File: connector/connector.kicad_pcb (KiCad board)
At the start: 2 copper layers, 18.7 x 4.8 mm, 15 parts, among them P11 CONN_1, P12 CONN_1, P13 CONN_1, P14 CONN_1, P15 CONN_1, P21 CONN_1, P22 CONN_1, P23 CONN_1, P24 CONN_1, P25 CONN_1

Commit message: Set solder mask clearance to 0.
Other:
- rule pad_to_mask_clearance: 0.1016 -> 0
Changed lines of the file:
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@@
     (pad_size 0.6096 0.6096)
     (pad_drill 0.3556)
-    (pad_to_mask_clearance 0.1016)
+    (pad_to_mask_clearance 0)
     (aux_axis_origin 0 0)
     (visible_elements FFFFFF7F)
@@
   (gr_line (start 138.4 102.4) (end 140.4 102.4) (angle 90) (layer Edge.Cuts) (width 0.01))
   (gr_line (start 140.4 102.4) (end 140.4 100.8) (angle 90) (layer Edge.Cuts) (width 0.01))
+  (segment (start 141 99.3) (end 141.333333 99.633333) (width 0.733) (layer Front) (net 1))
+  (segment (start 141 98.95) (end 141 99.3) (width 0.733) (layer Front) (net 1))
+  (segment (start 141.983333 99.633333) (end 141.333333 99.633333) (width 0.733) (layer Back) (net 1))
   (segment (start 142.1 99.75) (end 141.983333 99.633333) (width 0.733) (layer Back) (net 1))
-  (segment (start 141.983333 99.633333) (end 141.333333 99.633333) (width 0.733) (layer Back) (net 1))
-  (segment (start 141 98.95) (end 141 99.3) (width 0.733) (layer Front) (net 1))
-  (segment (start 141 99.3) (end 141.333333 99.633333) (width 0.733) (layer Front) (net 1))
+  (segment (start 143.5 99.3) (end 143.833333 99.633333) (width 0.733) (layer Front) (net 2))
+  (segment (start 143.5 98.95) (end 143.5 99.3) (width 0.733) (layer Front) (net 2))
+  (segment (start 144.633333 99.633333) (end 143.833333 99.633333) (width 0.733) (layer Back) (net 2))
   (segment (start 144.75 99.75) (end 144.633333 99.633333) (width 0.733) (layer Back) (net 2))
-  (segment (start 144.633333 99.633333) (end 143.833333 99.633333) (width 0.733) (layer Back) (net 2))
-  (segment (start 143.5 98.95) (end 143.5 99.3) (width 0.733) (layer Front) (net 2))
-  (segment (start 143.5 99.3) (end 143.833333 99.633333) (width 0.733) (layer Front) (net 2))
+  (segment (start 146 99.3) (end 146.333333 99.633333) (width 0.733) (layer Front) (net 3))
+  (segment (start 146 98.95) (end 146 99.3) (width 0.733) (layer Front) (net 3))
+  (segment (start 147.283333 99.633333) (end 146.333333 99.633333) (width 0.733) (layer Back) (net 3))
   (segment (start 147.4 99.75) (end 147.283333 99.633333) (width 0.733) (layer Back) (net 3))
-  (segment (start 147.283333 99.633333) (end 146.333333 99.633333) (width 0.733) (layer Back) (net 3))
-  (segment (start 146 98.95) (end 146 99.3) (width 0.733) (layer Front) (net 3))
-  (segment (start 146 99.3) (end 146.333333 99.633333) (width 0.733) (layer Front) (net 3))
+  (segment (start 148.5 99.3) (end 148.833333 99.633333) (width 0.733) (layer Front) (net 4))
+  (segment (start 148.5 98.95) (end 148.5 99.3) (width 0.733) (layer Front) (net 4))
+  (segment (start 149.933333 99.633333) (end 148.833333 99.633333) (width 0.733) (layer Back) (net 4))
   (segment (start 150.05 99.75) (end 149.933333 99.633333) (width 0.733) (layer Back) (net 4))
-  (segment (start 149.933333 99.633333) (end 148.833333 99.633333) (width 0.733) (layer Back) (net 4))
-  (segment (start 148.5 98.95) (end 148.5 99.3) (width 0.733) (layer Front) (net 4))
-  (segment (start 148.5 99.3) (end 148.833333 99.633333) (width 0.733) (layer Front) (net 4))
+  (segment (start 151 99.299999) (end 151.333334 99.633333) (width 0.733) (layer Front) (net 5))
+  (segment (start 151 98.95) (end 151 99.299999) (width 0.733) (layer Front) (net 5))
+  (segment (start 152.583333 99.633333) (end 151.333334 99.633333) (width 0.733) (layer Back) (net 5))
   (segment (start 152.7 99.75) (end 152.583333 99.633333) (width 0.733) (layer Back) (net 5))
-  (segment (start 152.583333 99.633333) (end 151.333334 99.633333) (width 0.733) (layer Back) (net 5))
-  (segment (start 151 98.95) (end 151 99.299999) (width 0.733) (layer Front) (net 5))
-  (segment (start 151 99.299999) (end 151.333334 99.633333) (width 0.733) (layer Front) (net 5))
 )

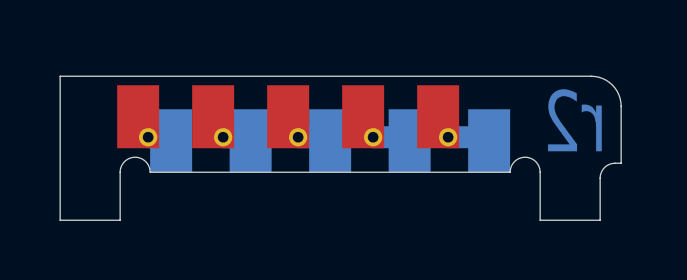
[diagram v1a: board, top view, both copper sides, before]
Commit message: Update outline.
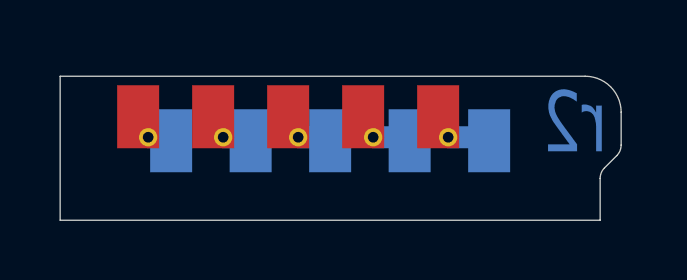
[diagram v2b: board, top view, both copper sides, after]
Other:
- outline, holes or cut-outs redrawn
- net class Default: clearance 0.01 -> 0.254; trace_width 0.889 -> 0.254
- rule trace_clearance: 0.01 -> 0.254
- rule trace_min: 0.6 -> 0.254
- rule via_min_drill: 0.635 -> 0.508

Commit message: Update pad positions.
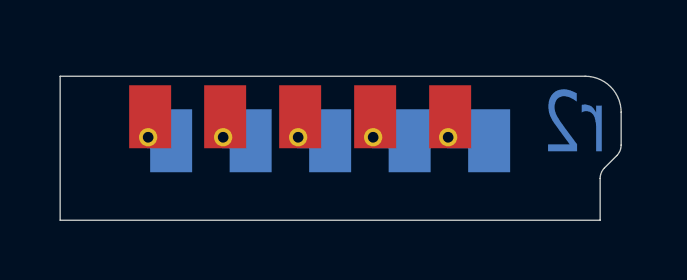
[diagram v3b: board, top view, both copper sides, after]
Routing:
- net N-000005: track 2.24 -> 1.41 mm
- net N-000003: track 1.94 -> 1.11 mm
- net N-000002: track 1.79 -> 0.96 mm
- net N-000001: track 1.64 -> 0.81 mm
- net N-000004: track 2.09 -> 1.26 mm
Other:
- rule pad_to_mask_clearance: 0 -> 0.254
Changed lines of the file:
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@@
     (thickness 1.6)
     (drawings 17)
-    (tracks 20)
+    (tracks 10)
     (zones 0)
     (modules 15)
@@
     (zone_45_only no)
     (trace_min 0.254)
-    (segment_width 0.2)
-    (edge_width 0.1)
+    (segment_width 0.381)
+    (edge_width 0.01016)
     (via_size 0.889)
     (via_drill 0.635)
@@
     (uvia_min_size 0.508)
     (uvia_min_drill 0.127)
-    (pcb_text_width 0.3)
-    (pcb_text_size 1.5 1.5)
-    (mod_edge_width 0.15)
-    (mod_text_size 1 1)
-    (mod_text_width 0.15)
-    (pad_size 1.5 1.5)
-    (pad_drill 0.6)
-    (pad_to_mask_clearance 0)
+    (pcb_text_width 0.3048)
+    (pcb_text_size 1.524 2.032)
+    (mod_edge_width 0.381)
+    (mod_text_size 1.524 1.524)
+    (mod_text_width 0.3048)
+    (pad_size 1.4 2.1)
+    (pad_drill 0)
+    (pad_to_mask_clearance 0.254)
     (aux_axis_origin 0 0)
     (visible_elements FFFFF77F)
@@
       (effects (font (thickness 0.3048)))
     )
-    (pad "" smd rect (at 0 0) (size 1.4 2.1) (layers F.Cu F.Mask)
+    (pad "" smd rect (at 0.4 0) (size 1.4 2.1) (layers F.Cu F.Mask)
       (net 5 N-000005))
   )
@@
       (effects (font (thickness 0.3048)))
     )
-    (pad "" smd rect (at 0 0) (size 1.4 2.1) (layers F.Cu F.Mask)
+    (pad "" smd rect (at 0.4 0) (size 1.4 2.1) (layers F.Cu F.Mask)
       (net 4 N-000004))
   )
@@
       (effects (font (thickness 0.3048)))
     )
-    (pad "" smd rect (at 0 0) (size 1.4 2.1) (layers F.Cu F.Mask)
+    (pad "" smd rect (at 0.4 0) (size 1.4 2.1) (layers F.Cu F.Mask)
       (net 3 N-000003))
   )
@@
       (effects (font (thickness 0.3048)))
     )
-    (pad "" smd rect (at 0 0) (size 1.4 2.1) (layers F.Cu F.Mask)
+    (pad "" smd rect (at 0.4 0) (size 1.4 2.1) (layers F.Cu F.Mask)
       (net 1 N-000001))
   )
@@
       (effects (font (thickness 0.3048)))
     )
-    (pad "" smd rect (at 0 0) (size 1.4 2.1) (layers F.Cu F.Mask)
+    (pad "" smd rect (at 0.4 0) (size 1.4 2.1) (layers F.Cu F.Mask)
       (net 2 N-000002))
   )
@@
   (segment (start 142.1 99.75) (end 141.983333 99.633333) (width 0.733) (layer B.Cu) (net 1))
   (segment (start 141.983333 99.633333) (end 141.333333 99.633333) (width 0.733) (layer B.Cu) (net 1))
-  (segment (start 141 98.95) (end 141 99.3) (width 0.733) (layer F.Cu) (net 1))
-  (segment (start 141 99.3) (end 141.333333 99.633333) (width 0.733) (layer F.Cu) (net 1))
   (segment (start 144.75 99.75) (end 144.633333 99.633333) (width 0.733) (layer B.Cu) (net 2))
   (segment (start 144.633333 99.633333) (end 143.833333 99.633333) (width 0.733) (layer B.Cu) (net 2))
-  (segment (start 143.5 98.95) (end 143.5 99.3) (width 0.733) (layer F.Cu) (net 2))
-  (segment (start 143.5 99.3) (end 143.833333 99.633333) (width 0.733) (layer F.Cu) (net 2))
   (segment (start 147.4 99.75) (end 147.283333 99.633333) (width 0.733) (layer B.Cu) (net 3))
   (segment (start 147.283333 99.633333) (end 146.333333 99.633333) (width 0.733) (layer B.Cu) (net 3))
-  (segment (start 146 98.95) (end 146 99.3) (width 0.733) (layer F.Cu) (net 3))
-  (segment (start 146 99.3) (end 146.333333 99.633333) (width 0.733) (layer F.Cu) (net 3))
   (segment (start 150.05 99.75) (end 149.933333 99.633333) (width 0.733) (layer B.Cu) (net 4))
   (segment (start 149.933333 99.633333) (end 148.833333 99.633333) (width 0.733) (layer B.Cu) (net 4))
-  (segment (start 148.5 98.95) (end 148.5 99.3) (width 0.733) (layer F.Cu) (net 4))
-  (segment (start 148.5 99.3) (end 148.833333 99.633333) (width 0.733) (layer F.Cu) (net 4))
   (segment (start 152.7 99.75) (end 152.583333 99.633333) (width 0.733) (layer B.Cu) (net 5))
   (segment (start 152.583333 99.633333) (end 151.333334 99.633333) (width 0.733) (layer B.Cu) (net 5))
-  (segment (start 151 98.95) (end 151 99.299999) (width 0.733) (layer F.Cu) (net 5))
-  (segment (start 151 99.299999) (end 151.333334 99.633333) (width 0.733) (layer F.Cu) (net 5))
 )

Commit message: Update the position of vias.
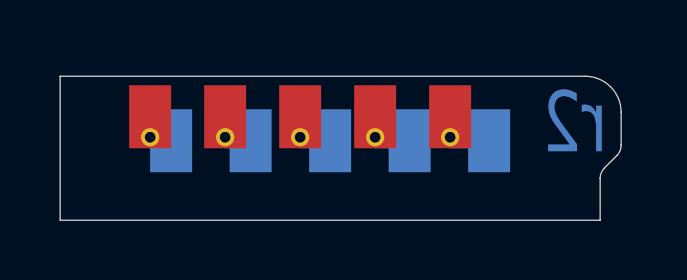
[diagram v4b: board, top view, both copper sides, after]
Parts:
- removed the via_24_14mil at (151.3, 99.6)
- removed the via_24_14mil at (148.8, 99.6)
- removed the via_24_14mil at (146.3, 99.6)
- removed the via_24_14mil at (143.8, 99.6)
- removed the via_24_14mil at (141.3, 99.6)
- added via_24_14mil: VAL**, UGL:via_24_14mil, F.Cu at (151.4, 99.6)
- added via_24_14mil: VAL**, UGL:via_24_14mil, F.Cu at (148.9, 99.6)
- added via_24_14mil: VAL**, UGL:via_24_14mil, F.Cu at (146.4, 99.6)
- added via_24_14mil: VAL**, UGL:via_24_14mil, F.Cu at (143.9, 99.6)
- added via_24_14mil: VAL**, UGL:via_24_14mil, F.Cu at (141.4, 99.6)
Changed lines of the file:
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@@
   )
   (setup
-    (last_trace_width 0.254)
+    (last_trace_width 0.733)
     (user_trace_width 0.733)
     (trace_clearance 0.254)
@@
     (mod_text_size 1.524 1.524)
     (mod_text_width 0.3048)
-    (pad_size 1.4 2.1)
-    (pad_drill 0)
+    (pad_size 0.6096 0.6096)
+    (pad_drill 0.3556)
     (pad_to_mask_clearance 0.254)
     (aux_axis_origin 0 0)
@@
   )
   (module UGL:via_24_14mil (layer F.Cu)
-    (at 151.333334 99.633333)
+    (at 151.4 99.633333)
     (fp_text reference via_24_14mil (at 0 -1.8) (layer F.SilkS) hide
       (effects (font (size 1 1) (thickness 0.15)))
@@
   )
   (module UGL:via_24_14mil (layer F.Cu)
-    (at 148.833333 99.633333)
+    (at 148.9 99.633333)
     (fp_text reference via_24_14mil (at 0 -1.8) (layer F.SilkS) hide
       (effects (font (size 1 1) (thickness 0.15)))
@@
   )
   (module UGL:via_24_14mil (layer F.Cu)
-    (at 146.333333 99.633333)
+    (at 146.4 99.633333)
     (fp_text reference via_24_14mil (at 0 -1.8) (layer F.SilkS) hide
       (effects (font (size 1 1) (thickness 0.15)))
@@
   )
   (module UGL:via_24_14mil (layer F.Cu)
-    (at 143.833333 99.633333)
+    (at 143.9 99.633333)
     (fp_text reference via_24_14mil (at 0 -1.8) (layer F.SilkS) hide
       (effects (font (size 1 1) (thickness 0.15)))
@@
   )
   (module UGL:via_24_14mil (layer F.Cu)
-    (at 141.333333 99.633333)
+    (at 141.4 99.633333)
     (fp_text reference via_24_14mil (at 0 -1.8) (layer F.SilkS) hide
       (effects (font (size 1 1) (thickness 0.15)))
@@
   (gr_line (start 156.4 101.007116) (end 156.4 102.4) (angle 90) (layer Edge.Cuts) (width 0.01))
   (segment (start 142.1 99.75) (end 141.983333 99.633333) (width 0.733) (layer B.Cu) (net 1))
-  (segment (start 141.983333 99.633333) (end 141.333333 99.633333) (width 0.733) (layer B.Cu) (net 1))
-  (segment (start 144.75 99.75) (end 144.633333 99.633333) (width 0.733) (layer B.Cu) (net 2))
-  (segment (start 144.633333 99.633333) (end 143.833333 99.633333) (width 0.733) (layer B.Cu) (net 2))
-  (segment (start 147.4 99.75) (end 147.283333 99.633333) (width 0.733) (layer B.Cu) (net 3))
-  (segment (start 147.283333 99.633333) (end 146.333333 99.633333) (width 0.733) (layer B.Cu) (net 3))
-  (segment (start 150.05 99.75) (end 149.933333 99.633333) (width 0.733) (layer B.Cu) (net 4))
-  (segment (start 149.933333 99.633333) (end 148.833333 99.633333) (width 0.733) (layer B.Cu) (net 4))
-  (segment (start 152.7 99.75) (end 152.583333 99.633333) (width 0.733) (layer B.Cu) (net 5))
-  (segment (start 152.583333 99.633333) (end 151.333334 99.633333) (width 0.733) (layer B.Cu) (net 5))
+  (segment (start 141.983333 99.633333) (end 141.4 99.633333) (width 0.733) (layer B.Cu) (net 1))
+  (segment (start 144.75 99.75) (end 144.633333 99.633333) (width 0.733) (layer B.Cu) (net 2) (status C00000))
+  (segment (start 144.633333 99.633333) (end 143.9 99.633333) (width 0.733) (layer B.Cu) (net 2) (status C00000))
+  (segment (start 147.4 99.75) (end 147.283333 99.633333) (width 0.733) (layer B.Cu) (net 3) (status C00000))
+  (segment (start 147.283333 99.633333) (end 146.4 99.633333) (width 0.733) (layer B.Cu) (net 3) (status C00000))
+  (segment (start 150.05 99.75) (end 149.933333 99.633333) (width 0.733) (layer B.Cu) (net 4) (status C00000))
+  (segment (start 149.933333 99.633333) (end 148.9 99.633333) (width 0.733) (layer B.Cu) (net 4) (status C00000))
+  (segment (start 152.7 99.75) (end 152.583333 99.633333) (width 0.733) (layer B.Cu) (net 5) (status C00000))
+  (segment (start 152.583333 99.633333) (end 151.4 99.633333) (width 0.733) (layer B.Cu) (net 5) (status C00000))
 )

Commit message: Update clearances.
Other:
- net class Default: trace_width 0.254 -> 0.7112; via_dia 0.889 -> 0.7112
- rule trace_min: 0.254 -> 0.7112
- rule via_min_size: 0.889 -> 0.7112
- board text added: "* design is 28mil-10mil-25mil trace-clearance-minimum_drill * 1mm board thickness * black soldermask * ENIG finish * no silkscreen"
- board text removed: "* design is 35mil-20mil-13mil trace-clearance-minimum_drill * 1mm board thickness * black soldermask * ENIG finish * no silkscreen"
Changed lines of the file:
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@@
   )
   (setup
-    (last_trace_width 0.733)
-    (user_trace_width 0.733)
+    (last_trace_width 0.7112)
+    (user_trace_width 0.7112)
     (trace_clearance 0.254)
     (zone_clearance 0.508)
     (zone_45_only no)
-    (trace_min 0.254)
+    (trace_min 0.7112)
     (segment_width 0.381)
     (edge_width 0.01016)
-    (via_size 0.889)
+    (via_size 0.7112)
     (via_drill 0.635)
-    (via_min_size 0.889)
+    (via_min_size 0.7112)
     (via_min_drill 0.508)
     (user_via 0.889 0.635)
@@
   (net_class Default "This is the default net class."
     (clearance 0.254)
-    (trace_width 0.254)
-    (via_dia 0.889)
+    (trace_width 0.7112)
+    (via_dia 0.7112)
     (via_drill 0.635)
     (uvia_dia 0.508)
@@
     (effects (font (size 2.032 1.524) (thickness 0.3048)) (justify mirror))
   )
-  (gr_text "* design is 35mil-20mil-13mil trace-clearance-minimum_drill\n* 1mm board thickness\n* black soldermask\n* ENIG finish\n* no silkscreen\n" (at 108.5 85) (layer Cmts.User)
+  (gr_text "* design is 28mil-10mil-25mil trace-clearance-minimum_drill\n* 1mm board thickness\n* black soldermask\n* ENIG finish\n* no silkscreen\n" (at 108.5 85) (layer Cmts.User)
     (effects (font (size 1.5 1.5) (thickness 0.3)) (justify left))
   )
@@
   (gr_line (start 156.4 102.4) (end 138.4 102.4) (angle 90) (layer Edge.Cuts) (width 0.01))
   (gr_line (start 156.4 101.007116) (end 156.4 102.4) (angle 90) (layer Edge.Cuts) (width 0.01))
+  (segment (start 141.983333 99.633333) (end 141.4 99.633333) (width 0.733) (layer B.Cu) (net 1))
   (segment (start 142.1 99.75) (end 141.983333 99.633333) (width 0.733) (layer B.Cu) (net 1))
-  (segment (start 141.983333 99.633333) (end 141.4 99.633333) (width 0.733) (layer B.Cu) (net 1))
-  (segment (start 144.75 99.75) (end 144.633333 99.633333) (width 0.733) (layer B.Cu) (net 2) (status C00000))
-  (segment (start 144.633333 99.633333) (end 143.9 99.633333) (width 0.733) (layer B.Cu) (net 2) (status C00000))
-  (segment (start 147.4 99.75) (end 147.283333 99.633333) (width 0.733) (layer B.Cu) (net 3) (status C00000))
-  (segment (start 147.283333 99.633333) (end 146.4 99.633333) (width 0.733) (layer B.Cu) (net 3) (status C00000))
-  (segment (start 150.05 99.75) (end 149.933333 99.633333) (width 0.733) (layer B.Cu) (net 4) (status C00000))
-  (segment (start 149.933333 99.633333) (end 148.9 99.633333) (width 0.733) (layer B.Cu) (net 4) (status C00000))
-  (segment (start 152.7 99.75) (end 152.583333 99.633333) (width 0.733) (layer B.Cu) (net 5) (status C00000))
-  (segment (start 152.583333 99.633333) (end 151.4 99.633333) (width 0.733) (layer B.Cu) (net 5) (status C00000))
+  (segment (start 144.633333 99.633333) (end 143.9 99.633333) (width 0.733) (layer B.Cu) (net 2))
+  (segment (start 144.75 99.75) (end 144.633333 99.633333) (width 0.733) (layer B.Cu) (net 2))
+  (segment (start 147.283333 99.633333) (end 146.4 99.633333) (width 0.733) (layer B.Cu) (net 3))
+  (segment (start 147.4 99.75) (end 147.283333 99.633333) (width 0.733) (layer B.Cu) (net 3))
+  (segment (start 149.933333 99.633333) (end 148.9 99.633333) (width 0.733) (layer B.Cu) (net 4))
+  (segment (start 150.05 99.75) (end 149.933333 99.633333) (width 0.733) (layer B.Cu) (net 4))
+  (segment (start 152.583333 99.633333) (end 151.4 99.633333) (width 0.733) (layer B.Cu) (net 5))
+  (segment (start 152.7 99.75) (end 152.583333 99.633333) (width 0.733) (layer B.Cu) (net 5))
 )
